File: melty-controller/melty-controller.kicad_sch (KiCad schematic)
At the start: 33 parts, among them J1 Conn_01x02_Male, J2 soicbite, J3 esc_io, Q1 2N7002ET1G, U1 ESP32-PICO-D4, U2 AIC1734-33GUTR, U3 MMA1200KEG, U4 HT7250

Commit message: experiments and stuff
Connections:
- net V5.0: now also U2.3 (VI)
- net VBAT: no longer U2.3 (VI)
- no-connect marks 10 -> 22
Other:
- note added: "Chain regulators to reduce power disspiation on 3.3v"
- moved on the sheet: C3, C5, U2, U4

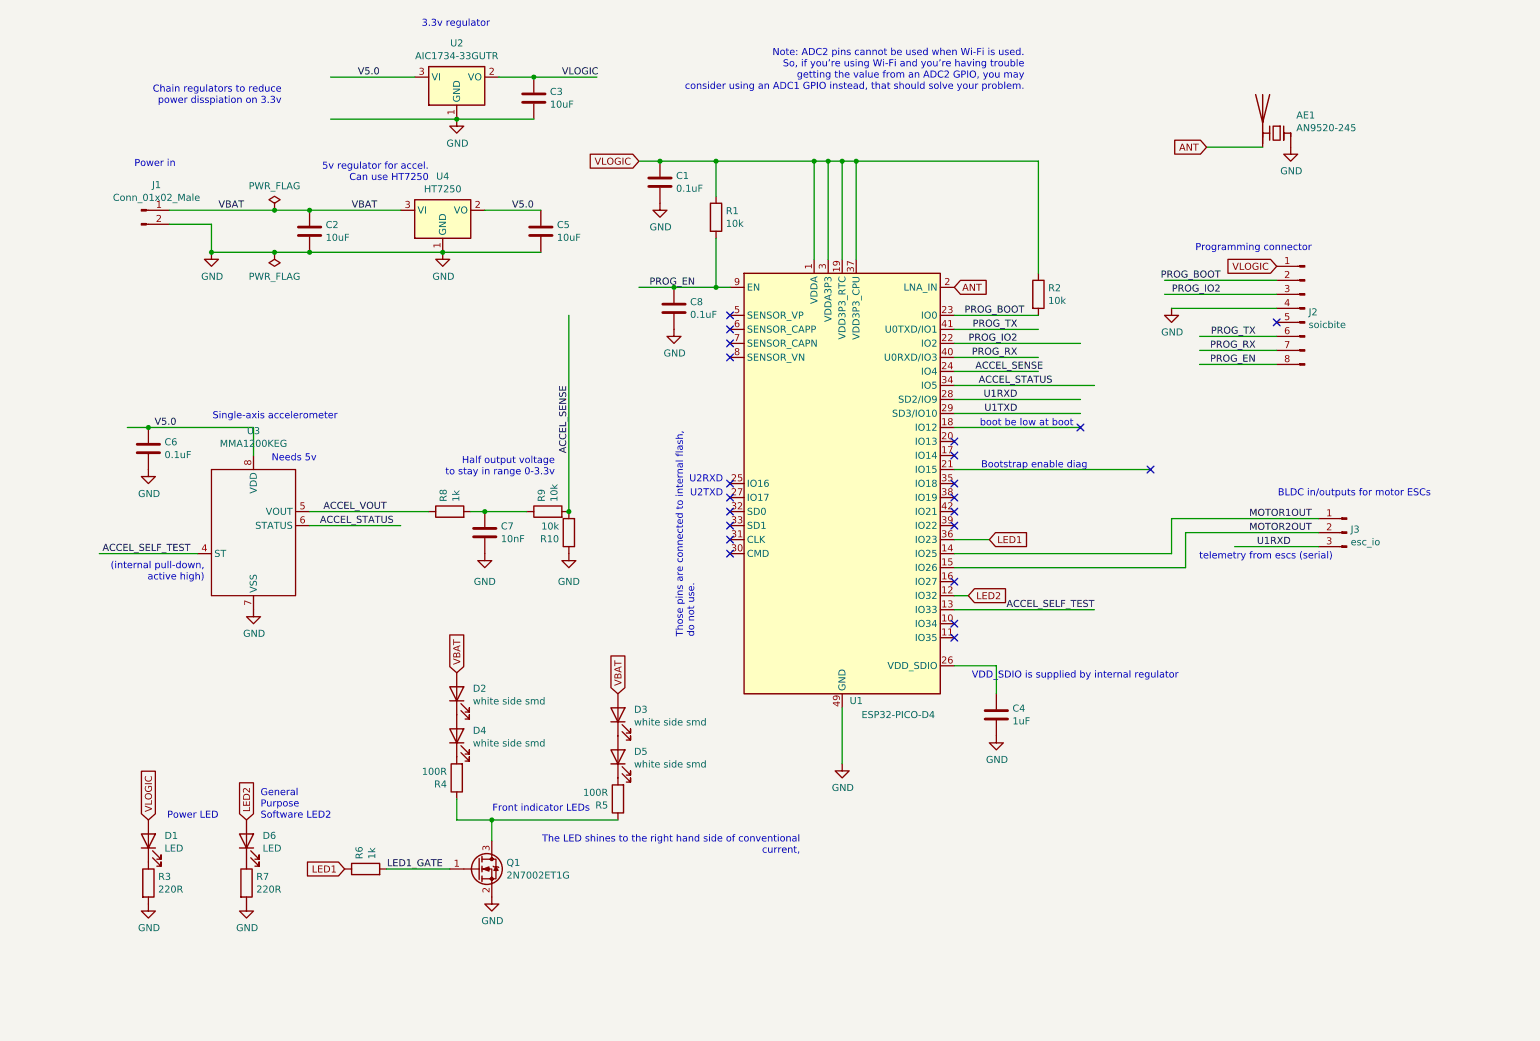
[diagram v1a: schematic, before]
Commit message: switcharoo power to bigger dual ldo regulators
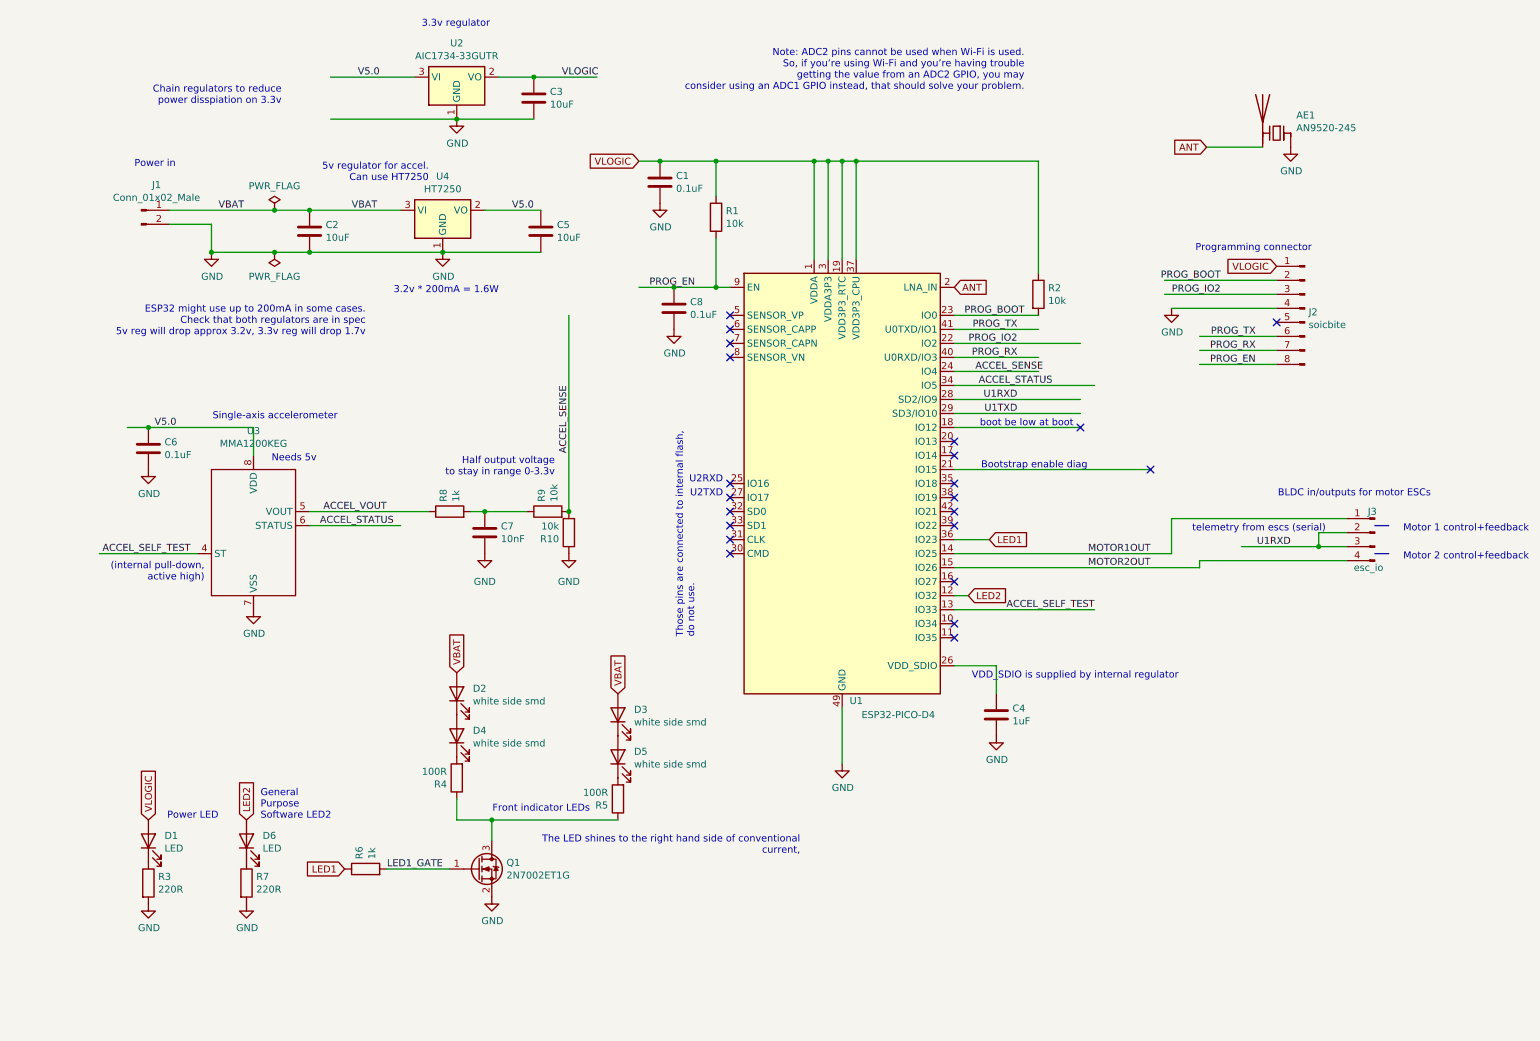
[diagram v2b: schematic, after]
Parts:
- removed J3: esc_io, Connector_PinHeader_2.54mm:PinHeader_1x03_P2.54mm_Vertical, symbol Connector:Conn_01x03_Male
- added J3: esc_io, Connector_PinHeader_2.00mm:PinHeader_1x04_P2.00mm_Vertical, symbol Connector:Conn_01x04_Male
- U2: footprint Package_TO_SOT_SMD:SOT-23 -> Package_TO_SOT_SMD:SOT-89-3; LCSC C211659 -> (none); Partnum C211659 -> (none)
- U4: footprint Package_TO_SOT_SMD:SOT-23 -> Package_TO_SOT_SMD:SOT-89-3
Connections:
- net MOTOR1OUT: now also J3.1 (Pin_1)
- net MOTOR2OUT: now also J3.4 (Pin_4)
- net U1RXD: now also J3.2 (Pin_2), J3.3 (Pin_3)
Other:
- note added: "3.2v * 200mA = 1.6W"
- note added: "ESP32 might use up to 200mA in some cases. Check that both regulators are in spec 5v reg will drop approx 3.2v, 3.3v reg will drop 1.7v"
- note added: "Motor 1 control+feedback"
- note added: "Motor 2 control+feedback"
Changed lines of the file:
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@@
   (junction (at 151.13 40.64) (diameter 0) (color 0 0 0 0))
   (junction (at 153.67 40.64) (diameter 0) (color 0 0 0 0))
+  (junction (at 237.49 110.49) (diameter 0) (color 0 0 0 0))
+  (no_connect (at 207.01 96.52))
   (no_connect (at 130.81 104.14))
+  (no_connect (at 171.45 127))
+  (no_connect (at 171.45 93.98))
+  (no_connect (at 130.81 71.12))
+  (no_connect (at 130.81 106.68))
+  (no_connect (at 130.81 99.06))
+  (no_connect (at 171.45 116.84))
+  (no_connect (at 130.81 111.76))
+  (no_connect (at 130.81 101.6))
+  (no_connect (at 171.45 99.06))
   (no_connect (at 229.87 69.85))
+  (no_connect (at 171.45 106.68))
+  (no_connect (at 171.45 91.44))
+  (no_connect (at 171.45 101.6))
   (no_connect (at 194.31 88.9))
-  (no_connect (at 207.01 96.52))
-  (no_connect (at 130.81 111.76))
+  (no_connect (at 130.81 73.66))
+  (no_connect (at 130.81 68.58))
+  (no_connect (at 171.45 104.14))
   (no_connect (at 130.81 109.22))
-  (no_connect (at 130.81 68.58))
-  (no_connect (at 130.81 71.12))
-  (no_connect (at 130.81 73.66))
+  (no_connect (at 171.45 124.46))
   (no_connect (at 130.81 76.2))
-  (no_connect (at 171.45 91.44))
-  (no_connect (at 171.45 93.98))
-  (no_connect (at 171.45 99.06))
-  (no_connect (at 171.45 101.6))
-  (no_connect (at 171.45 104.14))
-  (no_connect (at 171.45 106.68))
-  (no_connect (at 171.45 116.84))
-  (no_connect (at 171.45 124.46))
-  (no_connect (at 171.45 127))
-  (no_connect (at 130.81 101.6))
-  (no_connect (at 130.81 99.06))
-  (no_connect (at 130.81 106.68))
   (wire (pts (xy 16.51 111.76) (xy 34.29 111.76))
     (stroke (width 0) (type solid) (color 0 0 0 0))
@@
     (stroke (width 0) (type solid) (color 0 0 0 0))
   )
-  (wire (pts (xy 171.45 114.3) (xy 213.36 114.3))
+  (wire (pts (xy 171.45 114.3) (xy 215.9 114.3))
     (stroke (width 0) (type solid) (color 0 0 0 0))
   )
@@
     (stroke (width 0) (type solid) (color 0 0 0 0))
   )
-  (wire (pts (xy 210.82 105.41) (xy 237.49 105.41))
+  (wire (pts (xy 210.82 105.41) (xy 242.57 105.41))
     (stroke (width 0) (type solid) (color 0 0 0 0))
   )
@@
     (stroke (width 0) (type solid) (color 0 0 0 0))
   )
-  (wire (pts (xy 213.36 107.95) (xy 213.36 114.3))
-    (stroke (width 0) (type solid) (color 0 0 0 0))
-  )
-  (wire (pts (xy 213.36 107.95) (xy 237.49 107.95))
-    (stroke (width 0) (type solid) (color 0 0 0 0))
-  )
   (wire (pts (xy 215.9 72.39) (xy 229.87 72.39))
     (stroke (width 0) (type solid) (color 0 0 0 0))
@@
     (stroke (width 0) (type solid) (color 0 0 0 0))
   )
+  (wire (pts (xy 215.9 113.03) (xy 215.9 114.3))
+    (stroke (width 0) (type solid) (color 0 0 0 0))
+  )
   (wire (pts (xy 217.17 38.1) (xy 227.33 38.1))
     (stroke (width 0) (type solid) (color 0 0 0 0))
   )
-  (wire (pts (xy 222.25 110.49) (xy 237.49 110.49))
+  (wire (pts (xy 223.52 110.49) (xy 237.49 110.49))
+    (stroke (width 0) (type solid) (color 0 0 0 0))
+  )
+  (wire (pts (xy 237.49 107.95) (xy 237.49 110.49))
+    (stroke (width 0) (type solid) (color 0 0 0 0))
+  )
+  (wire (pts (xy 237.49 110.49) (xy 242.57 110.49))
+    (stroke (width 0) (type solid) (color 0 0 0 0))
+  )
+  (wire (pts (xy 242.57 107.95) (xy 237.49 107.95))
+    (stroke (width 0) (type solid) (color 0 0 0 0))
+  )
+  (wire (pts (xy 242.57 113.03) (xy 215.9 113.03))
+    (stroke (width 0) (type solid) (color 0 0 0 0))
+  )
+  (polyline (pts (xy 247.65 106.68) (xy 250.19 106.68))
+    (stroke (width 0) (type solid) (color 0 0 0 0))
+  )
+  (polyline (pts (xy 247.65 111.76) (xy 250.19 111.76))
     (stroke (width 0) (type solid) (color 0 0 0 0))
   )
@@
     (effects (font (size 1.27 1.27)) (justify right bottom))
   )
+  (text "ESP32 might use up to 200mA in some cases.\nCheck that both regulators are in spec\n5v reg will drop approx 3.2v, 3.3v reg will drop 1.7v"
+    (at 64.77 72.39 0)
+    (effects (font (size 1.27 1.27)) (justify right bottom))
+  )
   (text "3.3v regulator" (at 74.93 16.51 0)
     (effects (font (size 1.27 1.27)) (justify left bottom))
   )
   (text "5v regulator for accel.\nCan use HT7250" (at 76.2 44.45 180)
+    (effects (font (size 1.27 1.27)) (justify right bottom))
+  )
+  (text "3.2v * 200mA = 1.6W" (at 88.9 64.77 180)
     (effects (font (size 1.27 1.27)) (justify right bottom))
   )
@@
     (effects (font (size 1.27 1.27)) (justify right bottom))
   )
-  (text "telemetry from escs (serial)" (at 240.03 113.03 180)
+  (text "telemetry from escs (serial)" (at 238.76 107.95 180)
     (effects (font (size 1.27 1.27)) (justify right bottom))
   )
   (text "BLDC in/outputs for motor ESCs" (at 257.81 101.6 180)
+    (effects (font (size 1.27 1.27)) (justify right bottom))
+  )
+  (text "Motor 1 control+feedback" (at 275.59 107.95 180)
+    (effects (font (size 1.27 1.27)) (justify right bottom))
+  )
+  (text "Motor 2 control+feedback" (at 275.59 113.03 180)
     (effects (font (size 1.27 1.27)) (justify right bottom))
   )
@@
     (effects (font (size 1.27 1.27)) (justify right bottom))
   )
+  (label "MOTOR1OUT" (at 207.01 111.76 180)
+    (effects (font (size 1.27 1.27)) (justify right bottom))
+  )
+  (label "MOTOR2OUT" (at 207.01 114.3 180)
+    (effects (font (size 1.27 1.27)) (justify right bottom))
+  )
   (label "PROG_BOOT" (at 219.71 62.23 180)
     (effects (font (size 1.27 1.27)) (justify right bottom))
@@
   )
   (label "U1RXD" (at 232.41 110.49 180)
-    (effects (font (size 1.27 1.27)) (justify right bottom))
-  )
-  (label "MOTOR1OUT" (at 236.22 105.41 180)
-    (effects (font (size 1.27 1.27)) (justify right bottom))
-  )
-  (label "MOTOR2OUT" (at 236.22 107.95 180)
     (effects (font (size 1.27 1.27)) (justify right bottom))
   )
@@
     )
   )
-  (symbol (lib_id "Connector:Conn_01x03_Male") (at 242.57 107.95 0) (mirror y) (unit 1)
-    (in_bom yes) (on_board yes)
-    (property "Reference" "J3" (id 0) (at 243.2813 107.3594 0)
-      (effects (font (size 1.27 1.27)) (justify right))
-    )
-    (property "Value" "esc_io" (id 1) (at 243.2813 109.6581 0)
-      (effects (font (size 1.27 1.27)) (justify right))
-    )
-    (property "Footprint" "Connector_PinHeader_2.54mm:PinHeader_1x03_P2.54mm_Vertical" (id 2) (at 242.57 107.95 0)
-      (effects (font (size 1.27 1.27)) hide)
-    )
-    (property "Datasheet" "~" (id 3) (at 242.57 107.95 0)
+  (symbol (lib_id "Connector:Conn_01x04_Male") (at 247.65 107.95 0) (mirror y) (unit 1)
+    (in_bom yes) (on_board yes)
+    (property "Reference" "J3" (id 0) (at 246.38 104.14 0)
+      (effects (font (size 1.27 1.27)) (justify right))
+    )
+    (property "Value" "esc_io" (id 1) (at 243.84 114.3 0)
+      (effects (font (size 1.27 1.27)) (justify right))
+    )
+    (property "Footprint" "Connector_PinHeader_2.00mm:PinHeader_1x04_P2.00mm_Vertical" (id 2) (at 247.65 107.95 0)
+      (effects (font (size 1.27 1.27)) hide)
+    )
+    (property "Datasheet" "~" (id 3) (at 247.65 107.95 0)
       (effects (font (size 1.27 1.27)) hide)
     )
@@
     (property "Reference" "U4" (id 0) (at 78.74 43.3832 0))
     (property "Value" "HT7250" (id 1) (at 78.74 45.6946 0))
-    (property "Footprint" "Package_TO_SOT_SMD:SOT-23" (id 2) (at 78.74 45.72 0)
+    (property "Footprint" "Package_TO_SOT_SMD:SOT-89-3" (id 2) (at 78.74 45.72 0)
       (effects (font (size 1.27 1.27)) hide)
     )
@@
     (property "Reference" "U2" (id 0) (at 81.28 19.2532 0))
     (property "Value" "AIC1734-33GUTR" (id 1) (at 81.28 21.5646 0))
-    (property "Footprint" "Package_TO_SOT_SMD:SOT-23" (id 2) (at 81.28 21.59 0)
+    (property "Footprint" "Package_TO_SOT_SMD:SOT-89-3" (id 2) (at 81.28 21.59 0)
       (effects (font (size 1.27 1.27)) hide)
     )
@@
       (effects (font (size 1.27 1.27)) hide)
     )
-    (property "Partnum" "C211659" (id 4) (at 81.28 21.59 0)
-      (effects (font (size 1.27 1.27)) hide)
-    )
-    (property "LCSC" "C211659" (id 5) (at 81.28 21.59 0)
+    (property "Partnum" "" (id 4) (at 81.28 21.59 0)
+      (effects (font (size 1.27 1.27)) hide)
+    )
+    (property "LCSC" "" (id 5) (at 81.28 21.59 0)
       (effects (font (size 1.27 1.27)) hide)
     )
@@
       (reference "J2") (unit 1)
     )
-    (path "/9189e698-2631-4d7e-86d2-5c092e86aae1"
+    (path "/635acef9-2430-4621-9b86-cce3bee656a7"
       (reference "J3") (unit 1)
     )
